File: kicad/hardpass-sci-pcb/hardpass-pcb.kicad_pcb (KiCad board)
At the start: 2 copper layers, 80 x 65 mm, 50 parts, among them IC1 APX803, P1 Pi_Zero, P2 OLED_I2C, P3 Pi_Zero, SW1 1, SW10 C/UP, SW11 0/OK, SW12 OK/DN, SW2 2, SW3 3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

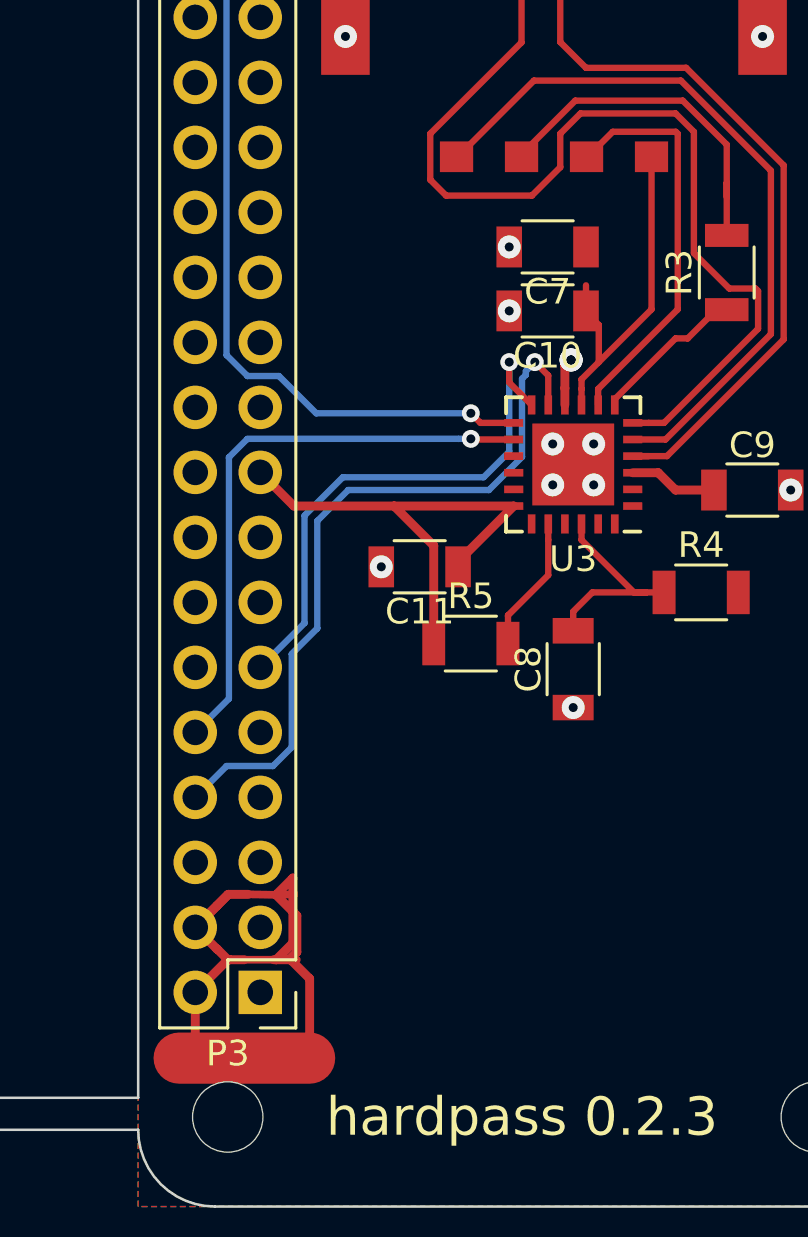
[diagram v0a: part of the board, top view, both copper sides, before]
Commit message: small fixes
schematic: add either-or text to card-led
pcb: connect c10 to card-pin1
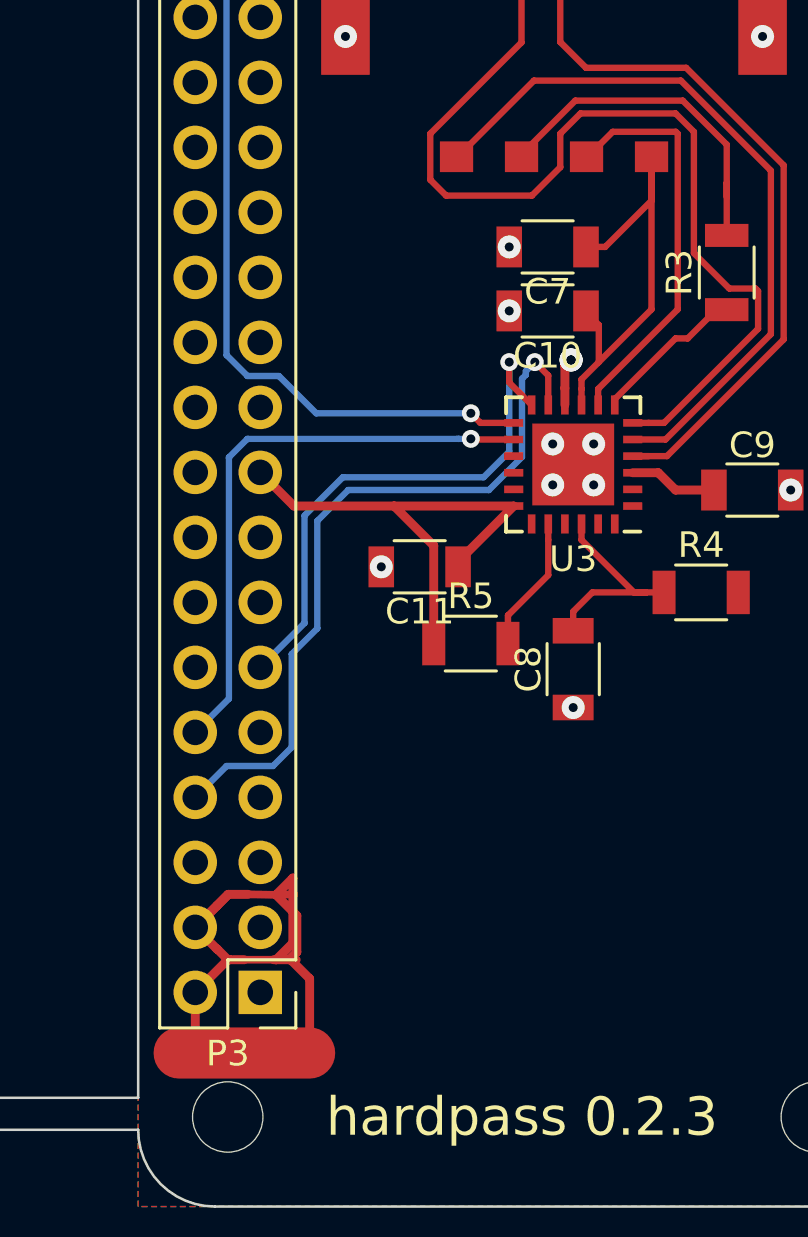
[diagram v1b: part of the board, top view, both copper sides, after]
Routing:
- net Net-(C10-Pad1): track 14.0 -> 18.0 mm
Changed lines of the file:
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@@
 (kicad_pcb (version 4) (host pcbnew 4.0.7-e2-6376~58~ubuntu16.04.1)
   (general
-    (links 156)
-    (no_connects 25)
-    (area -0.050001 -0.050001 80.050001 65.050001)
+    (links 153)
+    (no_connects 15)
+    (area -0.666014 -1.5255 80.050001 66.22418)
     (thickness 1.6)
     (drawings 27)
-    (tracks 733)
+    (tracks 736)
     (zones 0)
     (modules 50)
@@
     (add_net "Net-(C8-Pad2)")
     (add_net "Net-(D1-Pad1)")
-    (add_net "Net-(D1-Pad2)")
     (add_net "Net-(P1-Pad12)")
     (add_net "Net-(P1-Pad19)")
@@
   (segment (start 20.99 39.6) (end 22.5 38.09) (width 0.25) (layer B.Cu) (net 40))
   (segment (start 22.5 38.09) (end 22.5 37.45) (width 0.25) (layer B.Cu) (net 40))
-  (segment (start 51.6 59.2) (end 56.7 59.2) (width 2) (layer F.Cu) (net 63))
+  (segment (start 51.6 59) (end 56.7 59) (width 2) (layer F.Cu) (net 63))
   (segment (start 55.960001 55.354999) (end 55.392003 55.354999) (width 0.35) (layer F.Cu) (net 63))
   (segment (start 55.392003 55.354999) (end 55.3 55.354999) (width 0.35) (layer F.Cu) (net 63))
@@
   (segment (start 16.5 19.8) (end 13.95 22.35) (width 0.25) (layer B.Cu) (net 96))
   (segment (start 13.95 22.35) (end 13.95 23.7) (width 0.25) (layer B.Cu) (net 96))
+  (segment (start 67.5 27.5) (end 68.25 27.5) (width 0.25) (layer F.Cu) (net 97))
+  (segment (start 68.25 27.5) (end 70.06 25.69) (width 0.25) (layer F.Cu) (net 97))
+  (segment (start 70.06 25.69) (end 70.06 24.825) (width 0.25) (layer F.Cu) (net 97))
+  (segment (start 70.06 24.825) (end 70.06 23.975) (width 0.25) (layer F.Cu) (net 97))
   (segment (start 70.06 29.94) (end 68 32) (width 0.25) (layer F.Cu) (net 97))
   (segment (start 68 32) (end 67.325 32.675) (width 0.25) (layer F.Cu) (net 97))
   (segment (start 68 30.55) (end 68 32) (width 0.25) (layer F.Cu) (net 97))
-  (segment (start 67.5 29) (end 67.5 30.05) (width 0.25) (layer F.Cu) (net 97))
   (segment (start 67.5 30.05) (end 68 30.55) (width 0.25) (layer F.Cu) (net 97))
   (segment (start 70.06 23.975) (end 70.06 29.94) (width 0.25) (layer F.Cu) (net 97))

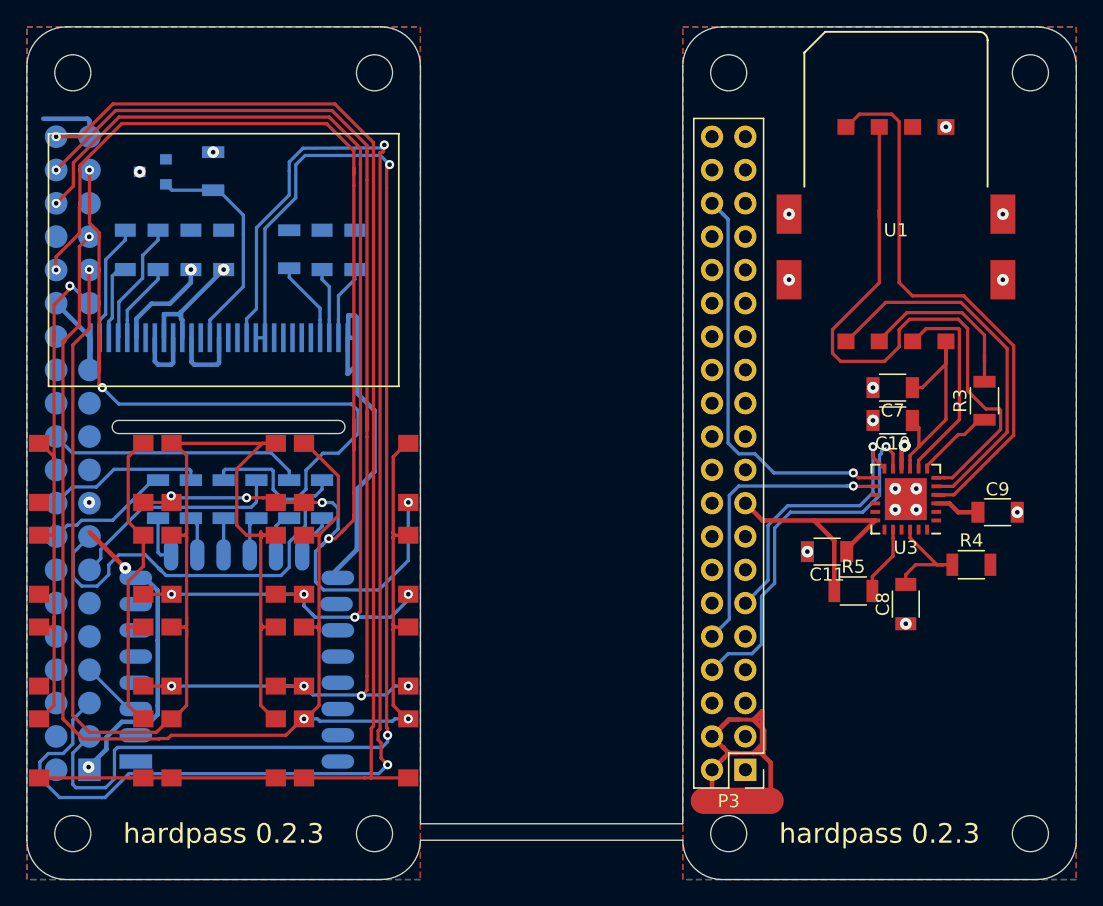
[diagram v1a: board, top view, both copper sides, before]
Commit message: seperate hardpass and hardpass-sci kicad projects
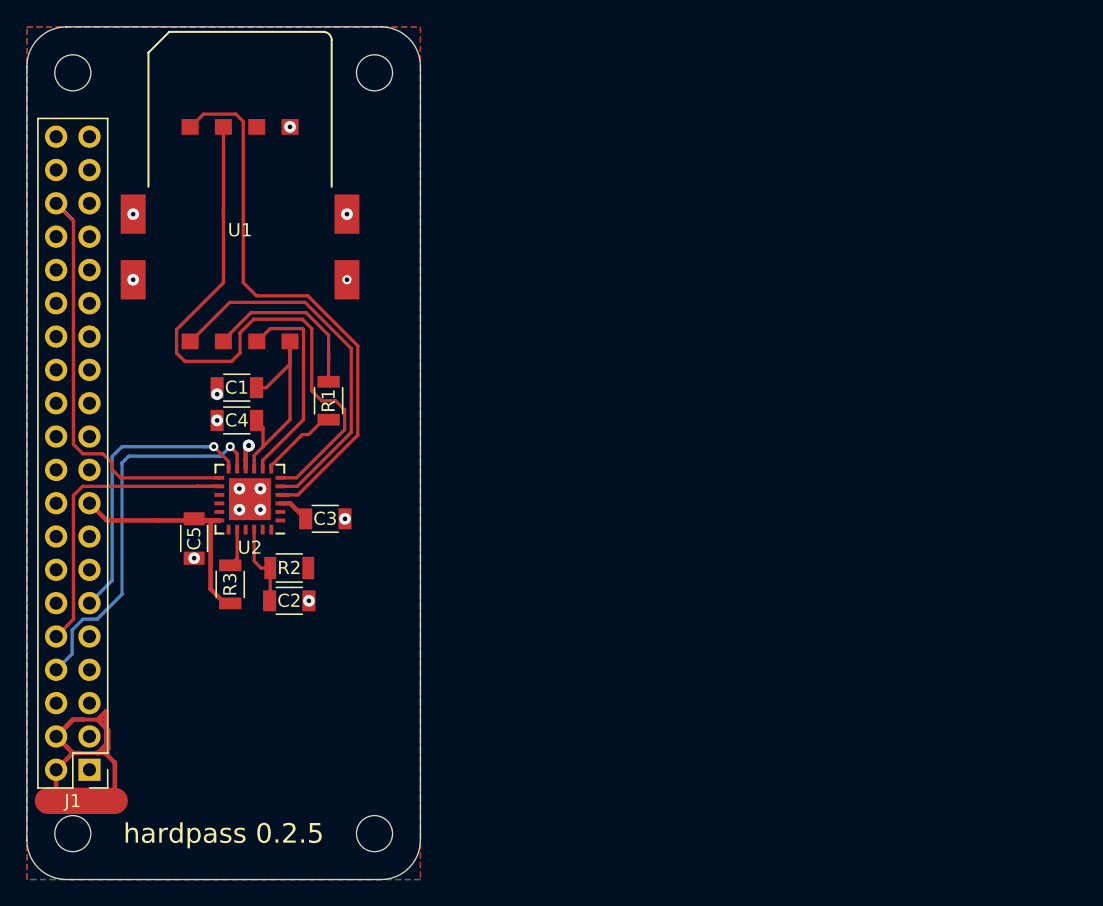
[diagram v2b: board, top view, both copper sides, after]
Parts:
- removed the ? at (26.5, 3.50)
- removed the ? at (26.5, 61.5)
- removed the ? at (3.50, 61.5)
- removed the ? at (3.50, 3.50)
- removed C10, C11, C9: 1µ, Capacitors_SMD:C_1206
- removed C6: 2.2µF, Capacitors_SMD:C_1206
- removed C7, C8: 100n, Capacitors_SMD:C_1206
- removed IC1: APX803, TO_SOT_Packages_SMD:SOT-23
- removed P1: Pi_Zero, hardpass:Pin_Header_Mirrored-NoHoles_centered_2x20
- removed P2: OLED_I2C, adafruit-oled:UG-2864HSWEG01_0.96IN_WRAPAROUND
- removed R12, R13, R14, R15, R16, R17: 33, Resistors_SMD:R_1206
- removed R4: 100K, Resistors_SMD:R_1206
- removed R5: 1M, Resistors_SMD:R_1206
- removed SW1: 1, hardpass:SW_SPST_PTS645_nosilk
- removed SW10: C/UP, hardpass:SW_SPST_PTS645_nosilk
- removed SW11: 0/OK, hardpass:SW_SPST_PTS645_nosilk
- removed SW12: OK/DN, hardpass:SW_SPST_PTS645_nosilk
- removed SW2: 2, hardpass:SW_SPST_PTS645_nosilk
- removed SW3: 3, hardpass:SW_SPST_PTS645_nosilk
- removed SW4: 4, hardpass:SW_SPST_PTS645_nosilk
- removed SW5: 5, hardpass:SW_SPST_PTS645_nosilk
- removed SW6: 6, hardpass:SW_SPST_PTS645_nosilk
- removed SW7: 7, hardpass:SW_SPST_PTS645_nosilk
- removed SW8: 8, hardpass:SW_SPST_PTS645_nosilk
- removed SW9: 9, hardpass:SW_SPST_PTS645_nosilk
- removed the U2 at (9.00, 56.0)
- C1, C2: value 2.2µF -> 100n; moved to F.Cu
- C3: value 10µF -> 1µ; moved to F.Cu
- C4, C5: value 2.2µF -> 1µ; moved to F.Cu
- J1: renamed from P3; value Pi_Zero -> Raspberry_Pi_2_3
- R1: value 390k -> 43; moved to F.Cu
- R2: value 10k -> 100K; moved to F.Cu
- R3: value 43 -> 1M
- moved R3 59.2 mm to (15.5, 42.5)
- moved ? 50.0 mm to (3.50, 61.5)
- moved ? 50.0 mm to (26.5, 61.5)
- moved ? 50.0 mm to (26.5, 3.50)
- moved ? 50.0 mm to (3.50, 3.50)
- moved J1 50.0 mm to (3.50, 32.5)
- moved REF** 50.0 mm to (15.0, 21.2)
- moved U1 50.0 mm to (16.2, 16.0)
- moved U2 50.0 mm to (17.0, 36.0)
- moved R2 30.8 mm to (20.0, 41.2), turned to 0 degrees
- moved C2 27.2 mm to (20.0, 43.8), turned to 180 degrees
- moved C5 22.2 mm to (12.8, 39.0)
- moved C3 20.6 mm to (22.8, 37.5), turned to 0 degrees
- moved C4 14.5 mm to (16.0, 30.0), turned to 180 degrees
- moved R1 11.9 mm to (23.0, 28.5)
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- renumbered U3 to U2
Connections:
- C1 pad 1: GND -> Net-(C1-Pad1)
- C1 pad 2: +3V3 -> GND
- C2 pad 2: +3V3 -> Net-(C2-Pad2)
- C3 pad 1: Net-(C3-Pad1) -> +5V
- C4 pad 1: Net-(C4-Pad1) -> Net-(C1-Pad1)
- C5 pad 1: Net-(C5-Pad1) -> +3V3
- C5 pad 2: Net-(C5-Pad2) -> GND
- R1 pad 1: Net-(P2-Pad26) -> Net-(R1-Pad1)
- R1 pad 2: GND -> Net-(R1-Pad2)
- R2 pad 1: +3V3 -> Net-(C2-Pad2)
- R2 pad 2: OLED_RST -> +5V
- R3 pad 1: Net-(R3-Pad1) -> +3V3
- R3 pad 2: Net-(R3-Pad2) -> Net-(D1-Pad1)
- U1 pad 1: Net-(C10-Pad1) -> Net-(C1-Pad1)
- U1 pad 3: Net-(R3-Pad2) -> Net-(R1-Pad2)
- U2 pad 22: Net-(C8-Pad2) -> Net-(C2-Pad2)
- U2 pad 7: Net-(R3-Pad1) -> Net-(R1-Pad1)
- U2 pad 9: Net-(C10-Pad1) -> Net-(C1-Pad1)
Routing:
- net COL_3: track 116.8 -> 0.00 mm, vias 3 -> 0
- net COL_2: track 107.6 -> 0.00 mm, vias 1 -> 0
- net OLED_SCL: track 106.8 -> 0.00 mm, vias 2 -> 0
- net ROW_4: track 103.6 -> 0.00 mm, vias 1 -> 0
- net OLED_SDA: track 97.7 -> 0.00 mm, vias 2 -> 0
- net ROW_3: track 93.4 -> 0.00 mm, vias 5 -> 0
- net ROW_1: track 72.7 -> 0.00 mm, vias 5 -> 0
- net COL_1: track 67.7 -> 0.00 mm, vias 1 -> 0
- net UART_CTS: track 65.0 -> 0.00 mm, vias 1 -> 0
- net SD_D2: track 57.4 -> 0.00 mm, vias 2 -> 0
- net ROW_2: track 55.9 -> 0.00 mm, vias 5 -> 0
- net GND: track 56.4 -> 4.21 mm
- net +3V3: track 62.1 -> 19.6 mm, vias 7 -> 0
- net ESP_CLK: track 30.9 -> 0.00 mm
- net SD_D1: track 19.6 -> 0.00 mm
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- removed copper zone on F.Cu, net +3V3
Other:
- board size 80 x 65 mm -> 30 x 65 mm
- board text added: "hardpass 0.2.5"
- board text removed: "hardpass 0.2.3"

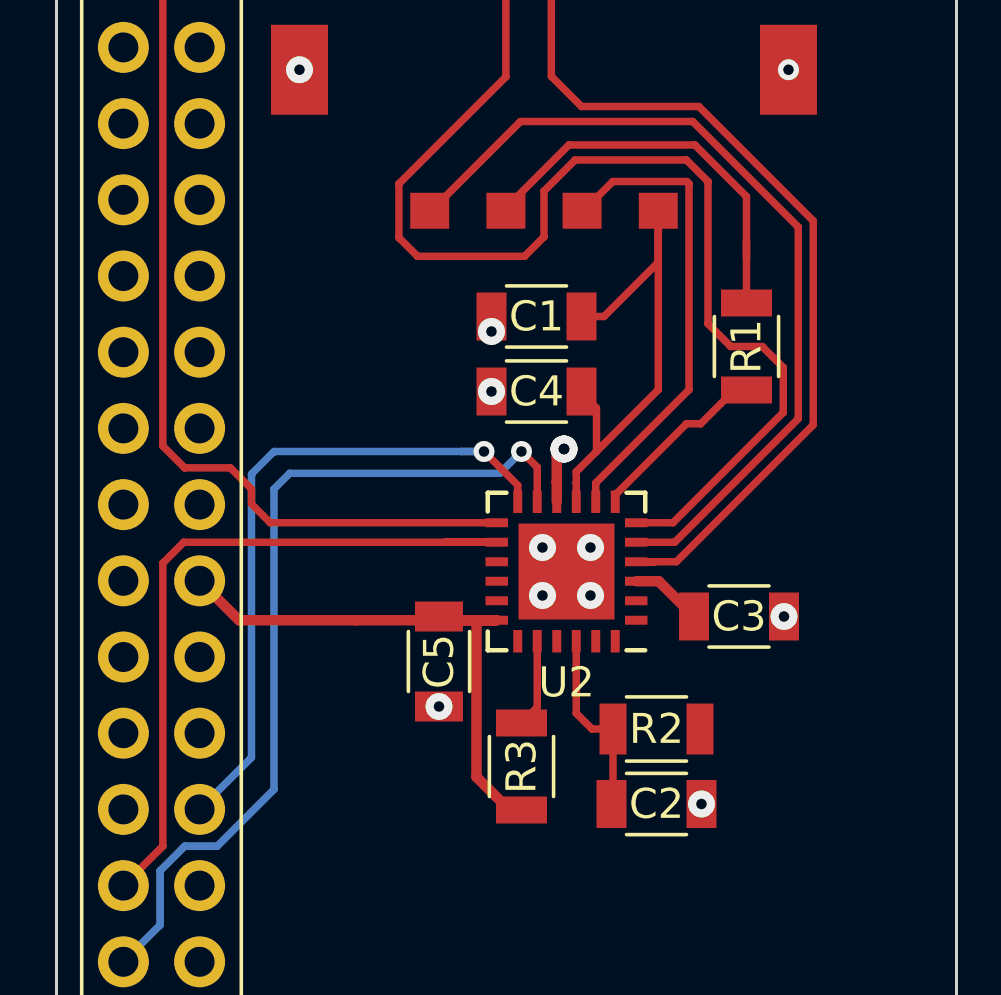
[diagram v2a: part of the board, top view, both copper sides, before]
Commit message: change sec1210 footprint to handsoldering
should ease qfn soldering by hand due to the elongated pads. this also
required moveing some traces out of the way on the pcb.
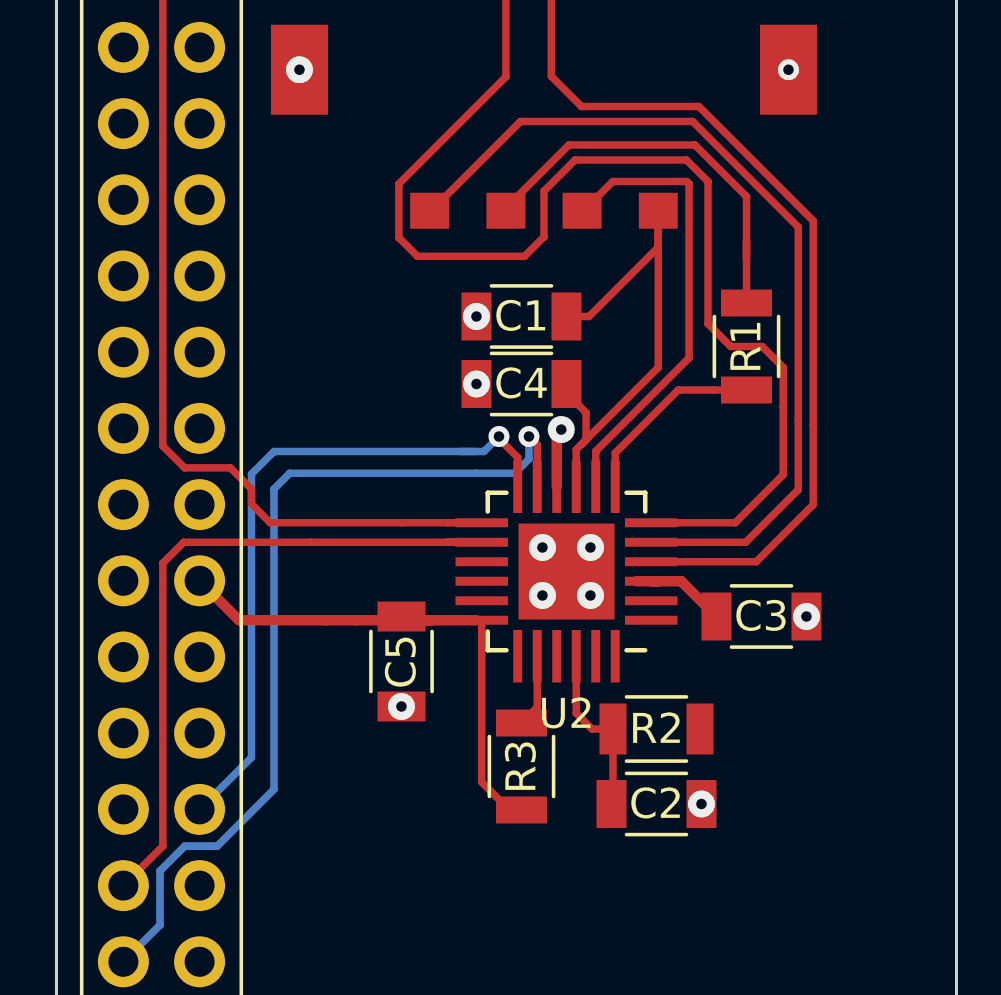
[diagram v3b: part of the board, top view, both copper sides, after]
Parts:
- U2: footprint Housings_DFN_QFN:QFN-24-1EP_5x5mm_Pitch0.65mm -> hardpass:QFN-24-1EP_5x5mm_Pitch0.65mm_HandSoldering
- moved C5 1.25 mm to (11.5, 39.0)
- moved C3 0.75 mm to (23.5, 37.5)
- moved C4 0.56 mm to (15.5, 29.8)
- moved C1 0.50 mm to (15.5, 27.5)
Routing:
- net Net-(U1-Pad8): track 42.9 -> 45.3 mm
- net Net-(U1-Pad4): track 28.5 -> 30.6 mm
- net Net-(U1-Pad7): track 48.2 -> 50.1 mm
- net +3V3: track 19.6 -> 17.9 mm
- net +5V: track 36.0 -> 37.0 mm
- net Net-(R1-Pad1): track 6.30 -> 7.24 mm
- net Net-(C1-Pad1): track 18.0 -> 18.9 mm
- net CARD_RX: track 29.1 -> 29.9 mm
- net GND: track 4.21 -> 3.57 mm, vias 16 -> 15
- net Net-(D1-Pad1): track 2.94 -> 2.44 mm
- net Net-(C2-Pad2): track 6.36 -> 5.86 mm
- net CARD_RTS: track 34.9 -> 34.4 mm
- net CARD_CTS: track 23.6 -> 24.1 mm
